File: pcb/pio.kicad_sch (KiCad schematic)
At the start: 32 parts, among them J11 GPA[0..3], J4 GPB[0..3], J5 GPB[4..7], J6 BTN[0..3], J7 GPA[4..7], U4 MCP23017T-E/ML

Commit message: Adjusted part values
Fixed LCSC footprints for connectors
Moved EN 5% instead of 1%
Moved I2C pull ups to 4.7K
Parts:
- J11, J6: LCSC C2763614 -> C2919601
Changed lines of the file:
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@@
 			)
 		)
-		(property "Description" "JST SH 1.0mm 4 Position"
+		(property "Description" "JST SH 1.0mm 4 Position Vertical"
 			(at 224.028 93.218 0)
 			(effects
@@
 			)
 		)
-		(property "LCSC" "C2763614"
+		(property "LCSC" "C2919601"
 			(at 224.028 83.82 0)
 			(effects
@@
 			)
 		)
-		(property "Description" "JST SH 1.0mm 6 Position"
+		(property "Description" "JST SH 1.0mm 6 Position Vertical"
 			(at 220.98 118.11 0)
 			(effects
@@
 			)
 		)
-		(property "Description" "JST SH 1.0mm 6 Position"
+		(property "Description" "JST SH 1.0mm 6 Position Vertical"
 			(at 220.98 41.91 0)
 			(effects
@@
 			)
 		)
-		(property "Description" "JST SH 1.0mm 4 Position"
+		(property "Description" "JST SH 1.0mm 4 Position Vertical"
 			(at 224.028 76.708 0)
 			(effects
@@
 			)
 		)
-		(property "LCSC" "C2763614"
+		(property "LCSC" "C2919601"
 			(at 224.028 67.31 0)
 			(effects
@@
 			)
 		)
-		(property "Description" "JST SH 1.0mm 6 Position"
+		(property "Description" "JST SH 1.0mm 6 Position Vertical"
 			(at 220.98 63.5 0)
 			(effects

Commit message: Cleaned up fab layer. Minor tweaks. Updated renders.
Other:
- note added: "GPIO Expander"
- moved on the sheet: C14, C9, D10, D11, D12, D13, D14, D15, D16, D17, D18, D19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

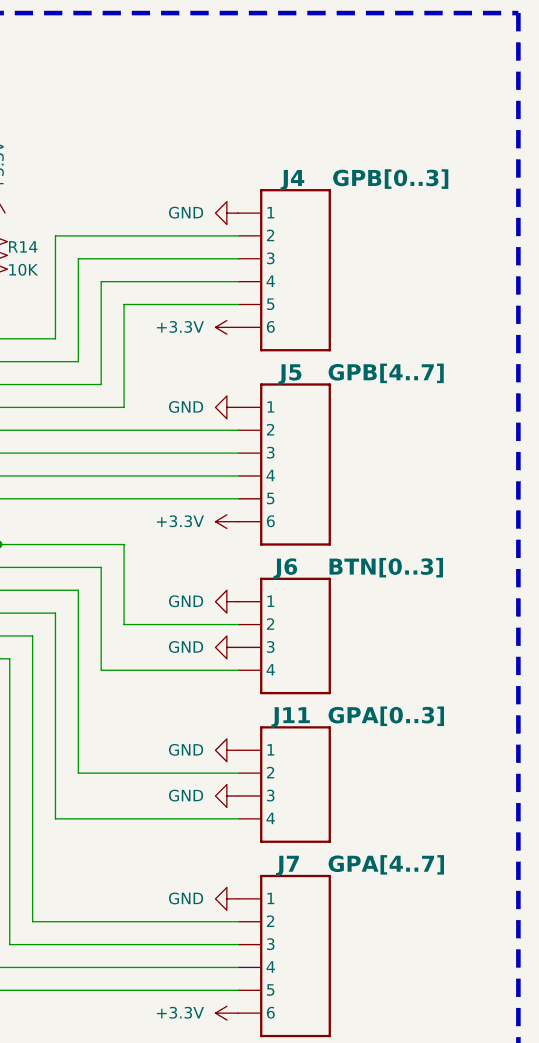
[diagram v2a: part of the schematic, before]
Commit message: closed #3 and #1
Fixed resistors and values
Widened panel
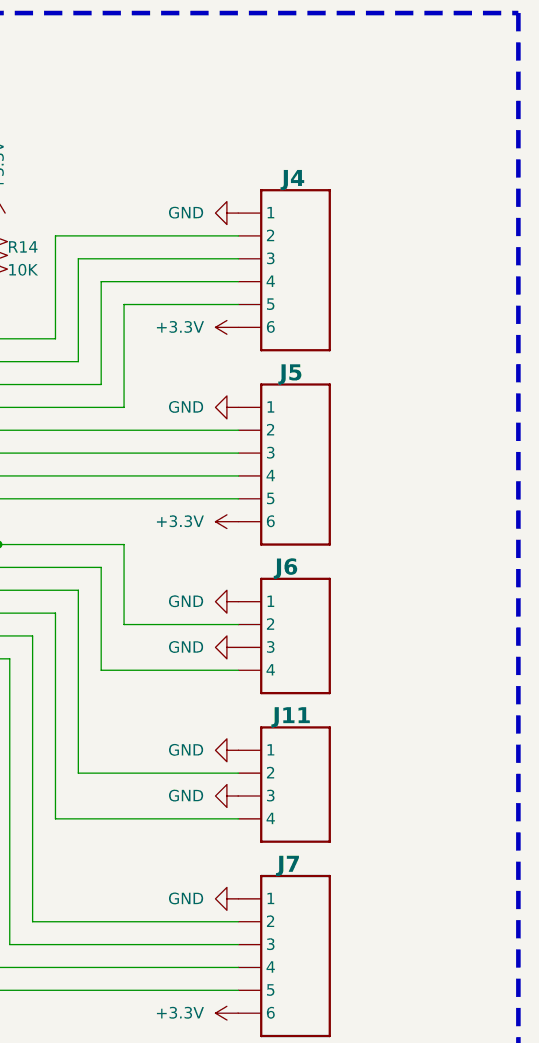
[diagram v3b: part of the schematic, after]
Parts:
- J11: value GPA[0..3] -> BM04B-SRSS-TB
- J4: value GPB[0..3] -> BM06B-SRSS-TB
- J5: value GPB[4..7] -> BM06B-SRSS-TB
- J6: value BTN[0..3] -> BM04B-SRSS-TB
- J7: value GPA[4..7] -> BM06B-SRSS-TB
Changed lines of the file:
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@@
 	(title_block
 		(title "Aquarius")
-		(date "2025-02-12")
-		(rev "1.5")
+		(date "2025-06-22")
+		(rev "2.0")
 		(company "CRG Makes")
 	)
@@
 			)
 		)
-		(property "Value" "GPA[0..3]"
+		(property "Value" "BM04B-SRSS-TB"
 			(at 210.566 94.996 0)
 			(effects
 				(font
 					(size 1.778 1.778)
-					(thickness 0.3556)
-					(bold yes)
+					(thickness 0.2223)
 				)
 				(justify left top)
+				(hide yes)
 			)
 		)
@@
 			)
 		)
-		(property "Value" "GPA[4..7]"
+		(property "Value" "BM06B-SRSS-TB"
 			(at 210.566 111.506 0)
 			(effects
 				(font
 					(size 1.778 1.778)
-					(thickness 0.3556)
-					(bold yes)
+					(thickness 0.2223)
 				)
 				(justify left bottom)
+				(hide yes)
 			)
 		)
@@
 			)
 		)
-		(property "Value" "GPB[0..3]"
+		(property "Value" "BM06B-SRSS-TB"
 			(at 211.074 35.306 0)
 			(effects
 				(font
 					(size 1.778 1.778)
-					(thickness 0.3556)
-					(bold yes)
+					(thickness 0.2223)
 				)
 				(justify left bottom)
+				(hide yes)
 			)
 		)
@@
 			)
 		)
-		(property "Value" "BTN[0..3]"
+		(property "Value" "BM04B-SRSS-TB"
 			(at 210.566 78.486 0)
 			(effects
 				(font
 					(size 1.778 1.778)
-					(thickness 0.3556)
-					(bold yes)
+					(thickness 0.2223)
 				)
 				(justify left top)
+				(hide yes)
 			)
 		)
@@
 			)
 		)
-		(property "Value" "GPB[4..7]"
+		(property "Value" "BM06B-SRSS-TB"
 			(at 210.566 56.896 0)
 			(effects
 				(font
 					(size 1.778 1.778)
-					(thickness 0.3556)
-					(bold yes)
+					(thickness 0.2223)
 				)
 				(justify left bottom)
+				(hide yes)
 			)
 		)
